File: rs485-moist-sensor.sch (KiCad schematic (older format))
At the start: 29 parts, among them IC1 ATTINY441-SSU, P1 CONN_02X03, P2 CONN_01X04, Q1 Q_PMOS_GSD, U1 SN65HVD72, U2 MCP1702, X1 16MHz

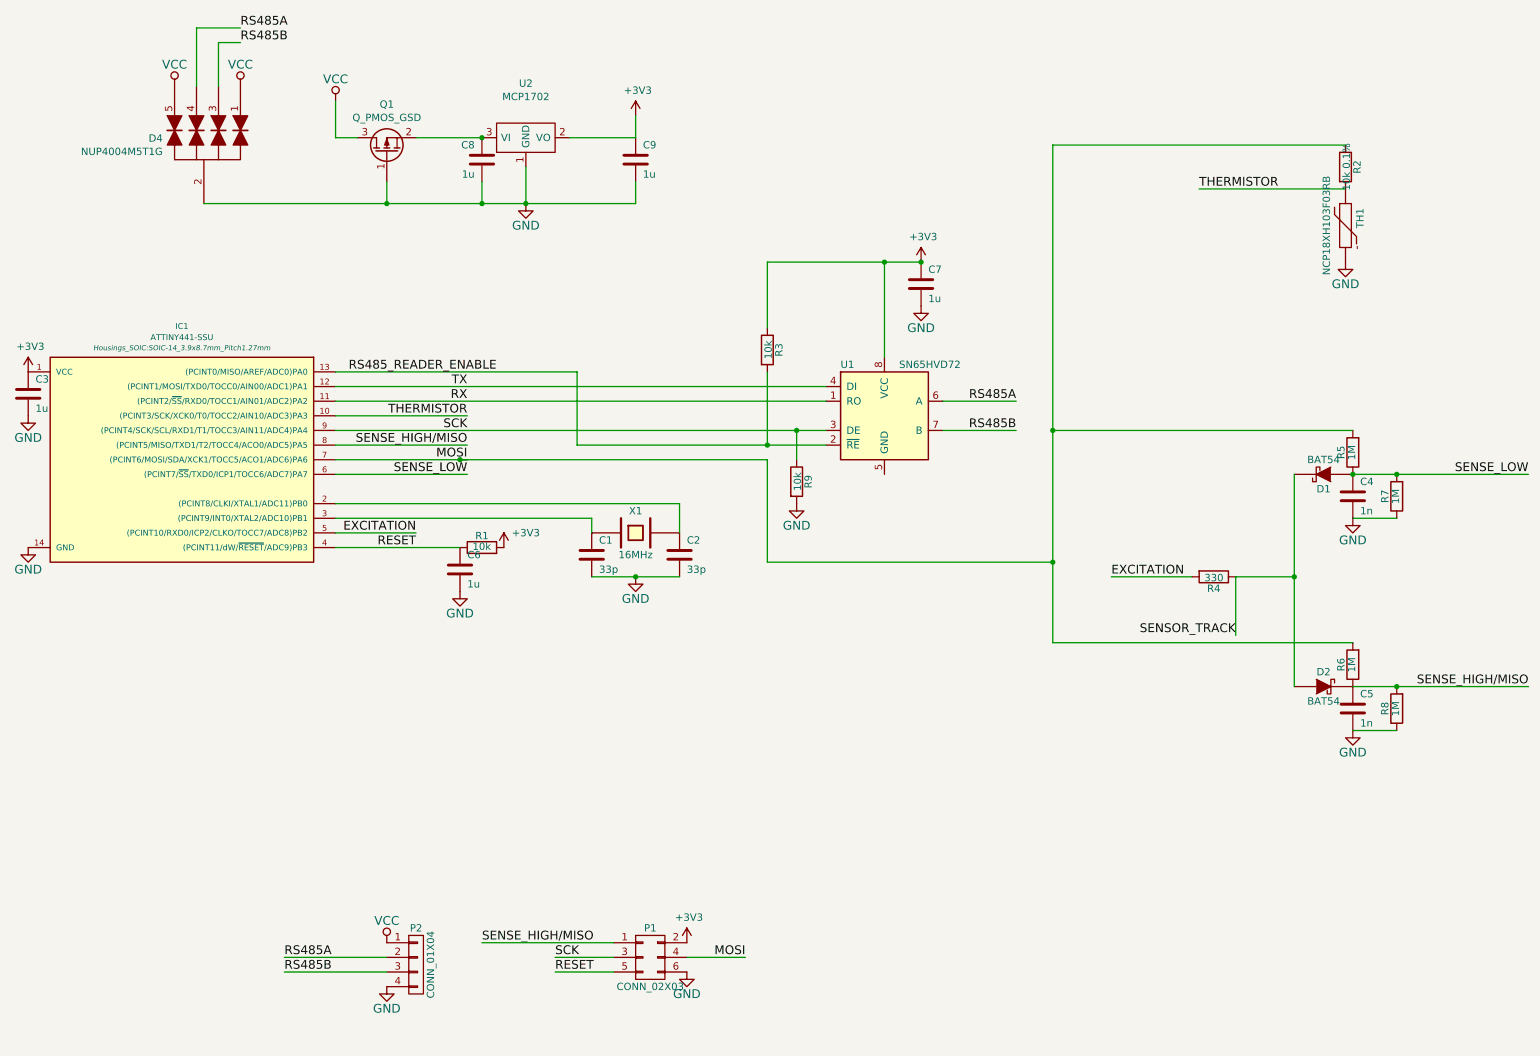
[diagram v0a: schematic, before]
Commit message: Fix a missing ground connection. Make PCB updatable from schematics directly
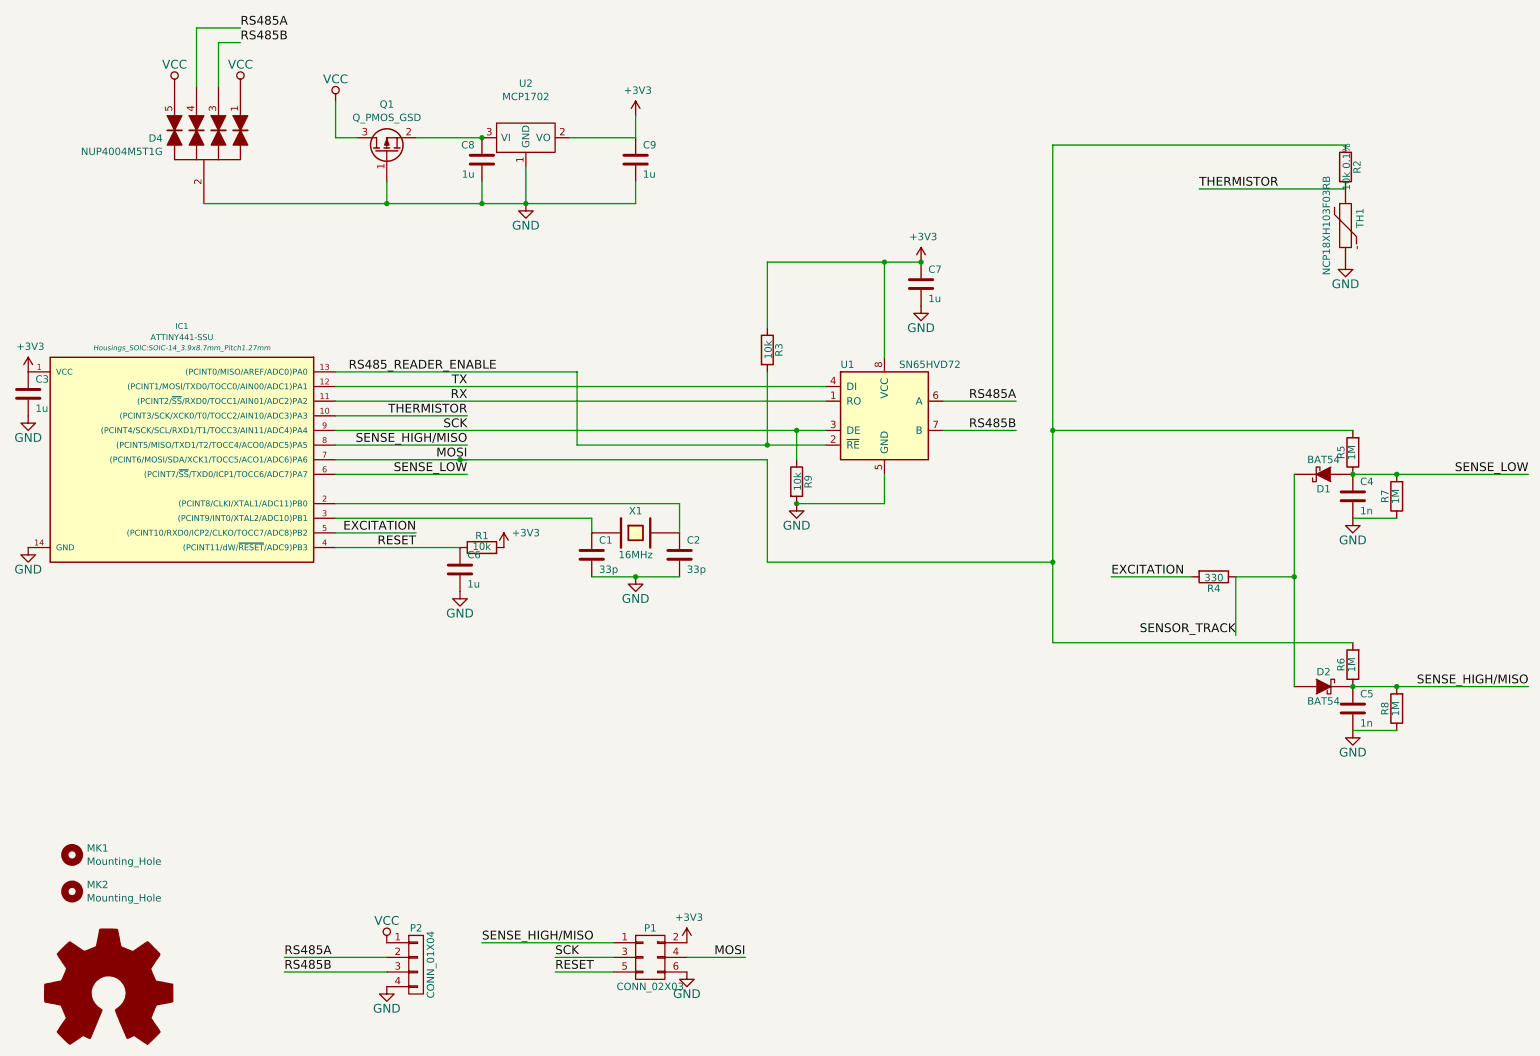
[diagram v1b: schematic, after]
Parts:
- added MK1, MK2: Mounting_Hole, Mounting_Holes:MountingHole_3mm, symbol Mounting_Hole
- Q1, U2: footprint Housings_SOT-23_SOT-143_TSOT-6:SOT-23_Handsoldering -> Housings_SOT-23_SOT-143_TSOT-6:SOT-23
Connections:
- net GND: now also U1.5 (GND)
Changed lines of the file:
@@
 LIBS:contrib
 LIBS:valves
+LIBS:mechanical
+LIBS:graphic_symbols
 LIBS:rs485-moist-sensor-cache
 EELAYER 26 0
@@
 $EndComp
 $Comp
-L GND #PWR01
+L GND #PWR13
 U 1 1 54D21A04
 P 4850 4500
-F 0 "#PWR01" H 4850 4250 60  0001 C CNN
+F 0 "#PWR13" H 4850 4250 60  0001 C CNN
 F 1 "GND" H 4850 4350 60  0000 C CNN
 F 2 "" H 4850 4500 60  0000 C CNN
@@
 $EndComp
 $Comp
-L VCC #PWR02
+L VCC #PWR6
 U 1 1 54D21DD5
 P 2800 1250
-F 0 "#PWR02" H 2800 1100 60  0001 C CNN
+F 0 "#PWR6" H 2800 1100 60  0001 C CNN
 F 1 "VCC" H 2800 1400 60  0000 C CNN
 F 2 "" H 2800 1250 60  0000 C CNN
@@
 $EndComp
 $Comp
-L GND #PWR03
+L GND #PWR3
 U 1 1 54D21DE7
 P 700 4300
-F 0 "#PWR03" H 700 4050 60  0001 C CNN
+F 0 "#PWR3" H 700 4050 60  0001 C CNN
 F 1 "GND" H 700 4150 60  0000 C CNN
 F 2 "" H 700 4300 60  0000 C CNN
@@
 $EndComp
 $Comp
-L GND #PWR04
+L GND #PWR2
 U 1 1 54D21F25
 P 700 3400
-F 0 "#PWR04" H 700 3150 60  0001 C CNN
+F 0 "#PWR2" H 700 3150 60  0001 C CNN
 F 1 "GND" H 700 3250 60  0000 C CNN
 F 2 "" H 700 3400 60  0000 C CNN
@@
 $EndComp
 $Comp
-L GND #PWR05
+L GND #PWR21
 U 1 1 54D2221D
 P 9750 5550
-F 0 "#PWR05" H 9750 5300 60  0001 C CNN
+F 0 "#PWR21" H 9750 5300 60  0001 C CNN
 F 1 "GND" H 9750 5400 60  0000 C CNN
 F 2 "" H 9750 5550 60  0000 C CNN
@@
 $EndComp
 $Comp
-L GND #PWR06
+L GND #PWR20
 U 1 1 54D222DF
 P 9750 4100
-F 0 "#PWR06" H 9750 3850 60  0001 C CNN
+F 0 "#PWR20" H 9750 3850 60  0001 C CNN
 F 1 "GND" H 9750 3950 60  0000 C CNN
 F 2 "" H 9750 4100 60  0000 C CNN
@@
 SENSOR_TRACK
 $Comp
-L GND #PWR07
+L GND #PWR15
 U 1 1 54D22F14
 P 5200 7200
-F 0 "#PWR07" H 5200 6950 60  0001 C CNN
+F 0 "#PWR15" H 5200 6950 60  0001 C CNN
 F 1 "GND" H 5200 7050 60  0000 C CNN
 F 2 "" H 5200 7200 60  0000 C CNN
@@
 $EndComp
 $Comp
-L GND #PWR08
+L GND #PWR18
 U 1 1 54DF0CCD
 P 6800 2650
-F 0 "#PWR08" H 6800 2400 60  0001 C CNN
+F 0 "#PWR18" H 6800 2400 60  0001 C CNN
 F 1 "GND" H 6800 2500 60  0000 C CNN
 F 2 "" H 6800 2650 60  0000 C CNN
@@
 $EndComp
 $Comp
-L GND #PWR09
+L GND #PWR16
 U 1 1 54DF15E6
 P 5950 4000
-F 0 "#PWR09" H 5950 3750 60  0001 C CNN
+F 0 "#PWR16" H 5950 3750 60  0001 C CNN
 F 1 "GND" H 5950 3850 60  0000 C CNN
 F 2 "" H 5950 4000 60  0000 C CNN
@@
 $EndComp
 $Comp
-L GND #PWR010
+L GND #PWR9
 U 1 1 54DF1D84
 P 3650 4600
-F 0 "#PWR010" H 3650 4350 60  0001 C CNN
+F 0 "#PWR9" H 3650 4350 60  0001 C CNN
 F 1 "GND" H 3650 4450 60  0000 C CNN
 F 2 "" H 3650 4600 60  0000 C CNN
@@
 $EndComp
 $Comp
-L GND #PWR011
+L GND #PWR19
 U 1 1 54E0608E
 P 9700 2350
-F 0 "#PWR011" H 9700 2100 60  0001 C CNN
+F 0 "#PWR19" H 9700 2100 60  0001 C CNN
 F 1 "GND" H 9700 2200 60  0000 C CNN
 F 2 "" H 9700 2350 60  0000 C CNN
@@
 $EndComp
 $Comp
-L VCC #PWR012
+L VCC #PWR7
 U 1 1 54E1FEA9
 P 3150 7000
-F 0 "#PWR012" H 3150 6850 60  0001 C CNN
+F 0 "#PWR7" H 3150 6850 60  0001 C CNN
 F 1 "VCC" H 3150 7150 60  0000 C CNN
 F 2 "" H 3150 7000 60  0000 C CNN
@@
 $EndComp
 $Comp
-L GND #PWR013
+L GND #PWR8
 U 1 1 54E1FECE
 P 3150 7300
-F 0 "#PWR013" H 3150 7050 60  0001 C CNN
+F 0 "#PWR8" H 3150 7050 60  0001 C CNN
 F 1 "GND" H 3150 7150 60  0000 C CNN
 F 2 "" H 3150 7300 60  0000 C CNN
@@
 $EndComp
 $Comp
-L GND #PWR014
+L GND #PWR11
 U 1 1 58946682
 P 4100 1950
-F 0 "#PWR014" H 4100 1700 60  0001 C CNN
+F 0 "#PWR11" H 4100 1700 60  0001 C CNN
 F 1 "GND" H 4100 1800 60  0000 C CNN
 F 2 "" H 4100 1950 60  0000 C CNN
@@
 	4850 1950 4850 1800
 $Comp
-L +3V3 #PWR015
+L +3V3 #PWR12
 U 1 1 5894698F
 P 4850 1350
-F 0 "#PWR015" H 2050 400 50  0001 C CNN
+F 0 "#PWR12" H 2050 400 50  0001 C CNN
 F 1 "+3V3" H 4865 1523 50  0000 C CNN
 F 2 "" H 2050 550 60  0000 C CNN
@@
 	4850 1500 4850 1350
 $Comp
-L +3V3 #PWR016
+L +3V3 #PWR1
 U 1 1 58946A8E
 P 700 3100
-F 0 "#PWR016" H -2100 2150 50  0001 C CNN
+F 0 "#PWR1" H -2100 2150 50  0001 C CNN
 F 1 "+3V3" H 715 3273 50  0000 C CNN
 F 2 "" H -2100 2300 60  0000 C CNN
@@
 $EndComp
 $Comp
-L +3V3 #PWR017
+L +3V3 #PWR17
 U 1 1 58946C25
 P 6800 2350
-F 0 "#PWR017" H 4000 1400 50  0001 C CNN
+F 0 "#PWR17" H 4000 1400 50  0001 C CNN
 F 1 "+3V3" H 6815 2523 50  0000 C CNN
 F 2 "" H 4000 1550 60  0000 C CNN
@@
 Connection ~ 6800 2350
 $Comp
-L +3V3 #PWR018
+L +3V3 #PWR14
 U 1 1 589472AD
 P 5200 7000
-F 0 "#PWR018" H 2400 6050 50  0001 C CNN
+F 0 "#PWR14" H 2400 6050 50  0001 C CNN
 F 1 "+3V3" H 5215 7173 50  0000 C CNN
 F 2 "" H 2400 6200 60  0000 C CNN
@@
 $EndComp
 $Comp
-L +3V3 #PWR019
+L +3V3 #PWR10
 U 1 1 58947B36
 P 3950 4300
-F 0 "#PWR019" H 1150 3350 50  0001 C CNN
+F 0 "#PWR10" H 1150 3350 50  0001 C CNN
 F 1 "+3V3" H 4100 4400 50  0000 C CNN
 F 2 "" H 1150 3500 60  0000 C CNN
@@
 F 0 "Q1" V 3478 1600 50  0000 C CNN
 F 1 "Q_PMOS_GSD" V 3387 1600 50  0000 C CNN
-F 2 "Housings_SOT-23_SOT-143_TSOT-6:SOT-23_Handsoldering" V 3600 1450 29  0001 C CNN
+F 2 "Housings_SOT-23_SOT-143_TSOT-6:SOT-23" V 3600 1450 29  0001 C CNN
 F 3 "" H 5450 850 60  0000 C CNN
 F 4 "NX2301P" H 3150 1600 60  0001 C CNN "PartNo"
@@
 F 0 "U2" H 4100 1871 50  0000 C CNN
 F 1 "MCP1702" H 4100 1780 50  0000 C CNN
-F 2 "Housings_SOT-23_SOT-143_TSOT-6:SOT-23_Handsoldering" H 4100 1681 60  0001 C CNN
+F 2 "Housings_SOT-23_SOT-143_TSOT-6:SOT-23" H 4100 1681 60  0001 C CNN
 F 3 "" H -1100 300 60  0000 C CNN
 F 4 "MCP1702T-3302E/CB" H 4100 1500 60  0001 C CNN "PartNo"
@@
 $EndComp
 $Comp
-L VCC #PWR020
+L VCC #PWR4
 U 1 1 58971B39
 P 1700 1150
-F 0 "#PWR020" H 1700 1000 60  0001 C CNN
+F 0 "#PWR4" H 1700 1000 60  0001 C CNN
 F 1 "VCC" H 1700 1300 60  0000 C CNN
 F 2 "" H 1700 1150 60  0000 C CNN
@@
 $EndComp
 $Comp
-L VCC #PWR021
+L VCC #PWR5
 U 1 1 58972379
 P 2150 1150
-F 0 "#PWR021" H 2150 1000 60  0001 C CNN
+F 0 "#PWR5" H 2150 1000 60  0001 C CNN
 F 1 "VCC" H 2150 1300 60  0000 C CNN
 F 2 "" H 2150 1150 60  0000 C CNN
@@
 	7700 4950 9750 4950
 Connection ~ 7700 4400
+Wire Wire Line
+	5950 4000 6550 4000
+Wire Wire Line
+	6550 4000 6550 3800
+Connection ~ 5950 4000
+Connection ~ 9750 5250
+$Comp
+L Mounting_Hole MK1
+U 1 1 59477C0A
+P 1000 6400
+F 0 "MK1" H 1100 6446 50  0000 L CNN
+F 1 "Mounting_Hole" H 1100 6355 50  0000 L CNN
+F 2 "Mounting_Holes:MountingHole_3mm" H 1000 6400 50  0001 C CNN
+F 3 "" H 1000 6400 50  0001 C CNN
+	1    1000 6400
+	1    0    0    -1
+$EndComp
+$Comp
+L Mounting_Hole MK2
+U 1 1 59477C98
+P 1000 6650
+F 0 "MK2" H 1100 6696 50  0000 L CNN
+F 1 "Mounting_Hole" H 1100 6605 50  0000 L CNN
+F 2 "Mounting_Holes:MountingHole_3mm" H 1000 6650 50  0001 C CNN
+F 3 "" H 1000 6650 50  0001 C CNN
+	1    1000 6650
+	1    0    0    -1
+$EndComp
+$Comp
+L Logo_Open_Hardware_Large #LOGO1
+U 1 1 594784A4
+P 1250 7350
+F 0 "#LOGO1" H 1250 7850 50  0001 C CNN
+F 1 "Logo_Open_Hardware_Large" H 1250 6950 50  0001 C CNN
+F 2 "w_logo:Logo_silk_OSHW_6x6mm" H 1250 7350 50  0001 C CNN
+F 3 "" H 1250 7350 50  0001 C CNN
+F 4 "?" H 1250 7350 60  0001 C CNN "PartNo"
+F 5 "?" H 1250 7350 60  0001 C CNN "Manufacturer"
+F 6 "?" H 1250 7350 60  0001 C CNN "Distributor"
+	1    1250 7350
+	1    0    0    -1
+$EndComp
 $EndSCHEMATC

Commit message: Update the sensor outline to accomodate narrower heatshrink. Also change ziptie application feature
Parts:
- C1, C2, C3, C4, C5, C6, C7, C8, C9: symbol C -> rs485-moist-sensor-rescue:C
- D1, D2: symbol DIODESCH -> rs485-moist-sensor-rescue:DIODESCH
- D4: symbol TVS-ARRAY -> rs485-moist-sensor-rescue:TVS-ARRAY
- IC1: symbol ATTINY441-SSU -> rs485-moist-sensor-rescue:ATTINY441-SSU
- MK1, MK2: symbol Mounting_Hole -> rs485-moist-sensor-rescue:Mounting_Hole
- P1: symbol CONN_02X03 -> rs485-moist-sensor-rescue:CONN_02X03
- P2: symbol CONN_01X04 -> rs485-moist-sensor-rescue:CONN_01X04
- Q1: symbol Q_PMOS_GSD-RESCUE-rs485-moist-sensor -> rs485-moist-sensor-rescue:Q_PMOS_GSD-RESCUE-rs485-moist-sensor
- R1, R2, R3, R4, R5, R6, R7, R8, R9: symbol R -> rs485-moist-sensor-rescue:R
- TH1: symbol THERMISTOR -> rs485-moist-sensor-rescue:THERMISTOR
- U1: symbol SP3481EN-RESCUE-rs485-moist-sensor -> rs485-moist-sensor-rescue:SP3481EN-RESCUE-rs485-moist-sensor
- U2: symbol MCP1702 -> rs485-moist-sensor-rescue:MCP1702
- X1: symbol CRYSTAL -> rs485-moist-sensor-rescue:CRYSTAL
